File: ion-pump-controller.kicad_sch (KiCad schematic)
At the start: 48 parts, among them J1 Barrel_Jack, J2 Conn_02x04_Counter_Clockwise, Q1 IRFP4668PbF, T1 Transformer_1P_1S, U1 TSR_1-2433, U2 MCP6001R, U3 TC4422, U4 TSR1.5-24120E

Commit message: 1.0 version
these are the new schematic and pcb files for what should be the theoretically working board
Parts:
- removed J2: Conn_02x04_Counter_Clockwise, symbol Connector_Generic:Conn_02x04_Counter_Clockwise
- removed U3: TC4422, Package_DIP:DIP-8_W7.62mm, symbol Driver_FET:TC4422
- added C9: 2.5nf, Capacitor_THT:C_Disc_D14.5mm_W5.0mm_P10.00mm, symbol Device:C
- added D9: UF5408, Diode_THT:D_DO-201AD_P15.24mm_Horizontal, symbol Diode:UF5408
- added J2: START BUTTON, TerminalBlock_Phoenix:TerminalBlock_Phoenix_MKDS-1,5-2_1x02_P5.00mm_Horizontal, symbol Connector:Conn_01x02_Pin
- added J3: SCREEN, Connector_Phoenix_SPT:PhoenixContact_SPT_2.5_4-H-5.0_1x04_P5.0mm_Horizontal, symbol Connector:Conn_01x04_Pin
- added J4: DRAIN BUTTON, TerminalBlock_Phoenix:TerminalBlock_Phoenix_MKDS-1,5-2_1x02_P5.00mm_Horizontal, symbol Connector:Conn_01x02_Pin
- added J5: LIGHT, TerminalBlock_Phoenix:TerminalBlock_Phoenix_MKDS-1,5-2_1x02_P5.00mm_Horizontal, symbol Connector:Conn_01x02_Pin
- added J6: POWER SWITCH, TerminalBlock_Phoenix:TerminalBlock_Phoenix_MKDS-1,5-2_1x02_P5.00mm_Horizontal, symbol Connector:Conn_01x02_Pin
- added R22, R23: 330, Resistor_THT:R_Axial_DIN0411_L9.9mm_D3.6mm_P25.40mm_Horizontal, symbol Device:R
- added R24: 1k, Resistor_THT:R_Axial_DIN0411_L9.9mm_D3.6mm_P25.40mm_Horizontal, symbol Device:R
- added R25: 47k, Resistor_THT:R_Axial_DIN0411_L9.9mm_D3.6mm_P25.40mm_Horizontal, symbol Device:R
- added U5: 6N137, Package_DIP:DIP-8_W7.62mm, symbol Isolator:6N137
- added U6: TC4421, Package_DIP:DIP-8_W7.62mm, symbol Driver_FET:TC4421
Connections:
- net +12V: now also U6.1 (VDD), U6.8 (VDD)
- net +24V: now also C9.1, J6.1 (Pin_1), R25.1; no longer J1.1
- net +3V3: now also J3.1 (Pin_1), R24.2, U5.7 (EN), U5.8 (VCC)
- net GND: now also J2.2 (Pin_2), J3.4 (Pin_4), J4.2 (Pin_2), J5.2 (Pin_2), U5.3 (C), U5.5 (GND), U6.4 (GND), U6.5 (GND)
- net PWM output: now also R23.2, U5.2 (A); no longer A1.5 (DAC2/A0)
- net at A1.17 (SDA/IO23): now also J3.2 (Pin_2)
- net at A1.18 (SCL/IO22): now also J3.3 (Pin_3)
- net at A1.19 (A6/IO14): now also J2.1 (Pin_1)
- net at A1.20 (A7/IO32): now also J4.1 (Pin_1)
- net at A1.23 (A10/IO27): now also R22.1
- net at Q1.1 (G): now also U6.6 (~{OUTPUT}), U6.7 (~{OUTPUT})
- net at Q1.2 (D), T1.2 (AB): now also D9.2 (A)
- new net: R24.1, U5.6 (VO), U6.2 (INPUT)
- new net: A1.5 (DAC2/A0), R23.1
- new net: J1.1, J6.2 (Pin_2)
- new net: C9.2, D9.1 (K), R25.2
- new net: J5.1 (Pin_1), R22.2
- no-connect marks 17 -> 18
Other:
- note added: "EVIL ASS HIGH VOLTAGE OWIE"
- note added: "MOCK - DIFFERENT WHEN REALIZED"
- note added: "THERE IS NO OUTPUT PUT THE OUTPUT TYPE YOU NEED FOR YOUR ION PUMP HERE"
- note added: "screen mock"
- note removed: "ADD 1 SCREEN WITH 4 LINES ADD 1 SWITCH FOR POWER ADD 2 BUTTONS FOR GO/DRAIN START - PIN 14 DRAIN - PIN 32 LIGHT - PIN 27 SCREEN - PIN 23, 22, VCC, GND"
- moved on the sheet: Q1, T1, U4

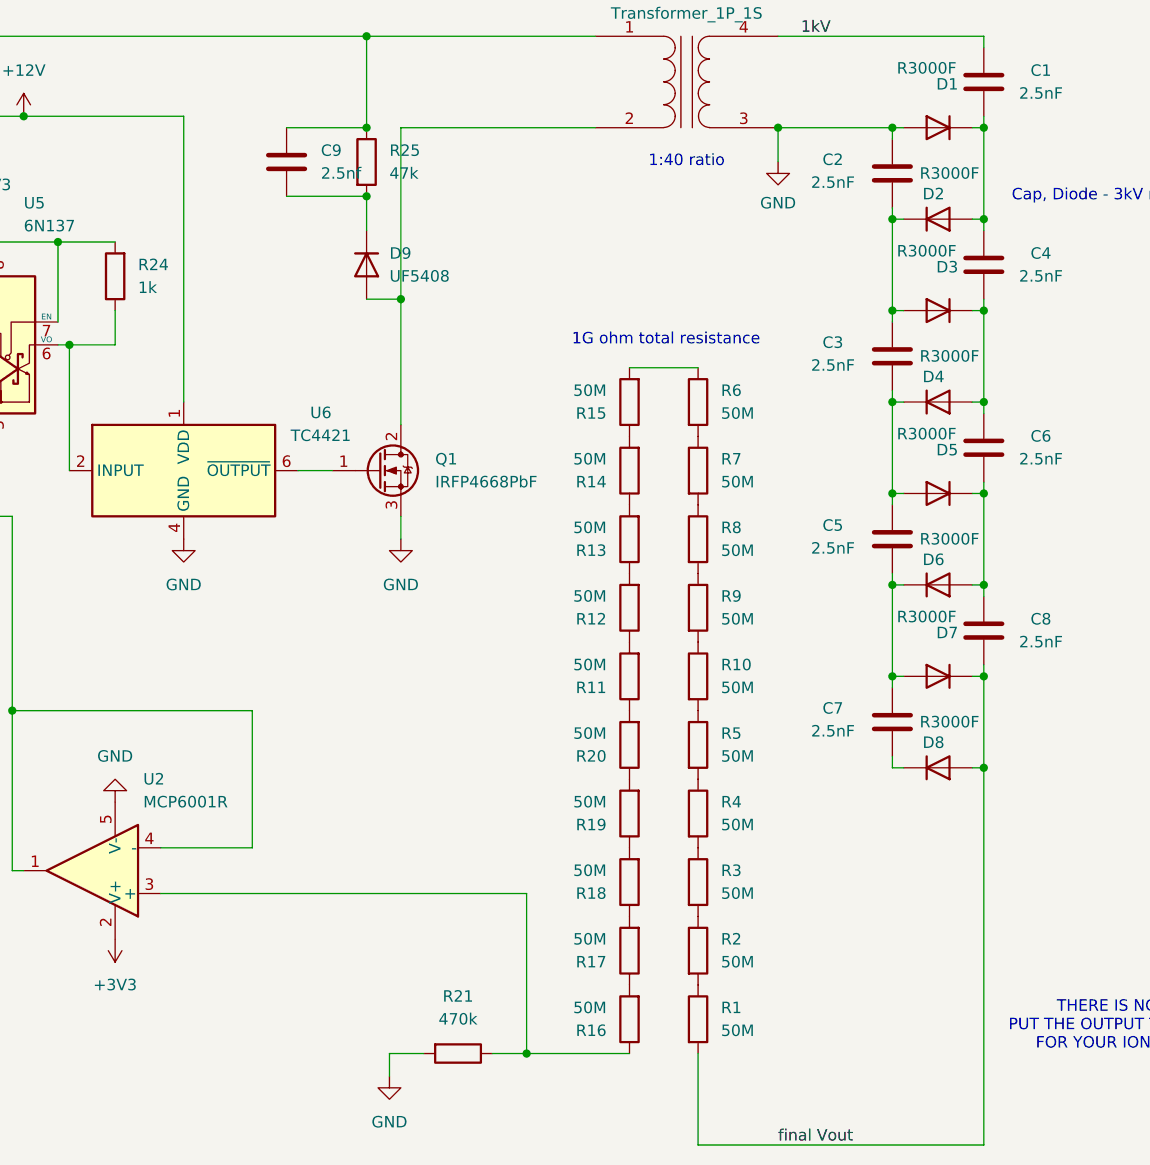
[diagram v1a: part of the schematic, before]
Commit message: v1.1
split the ground plane to high and low voltage, made the output two pads instead of screw terminals
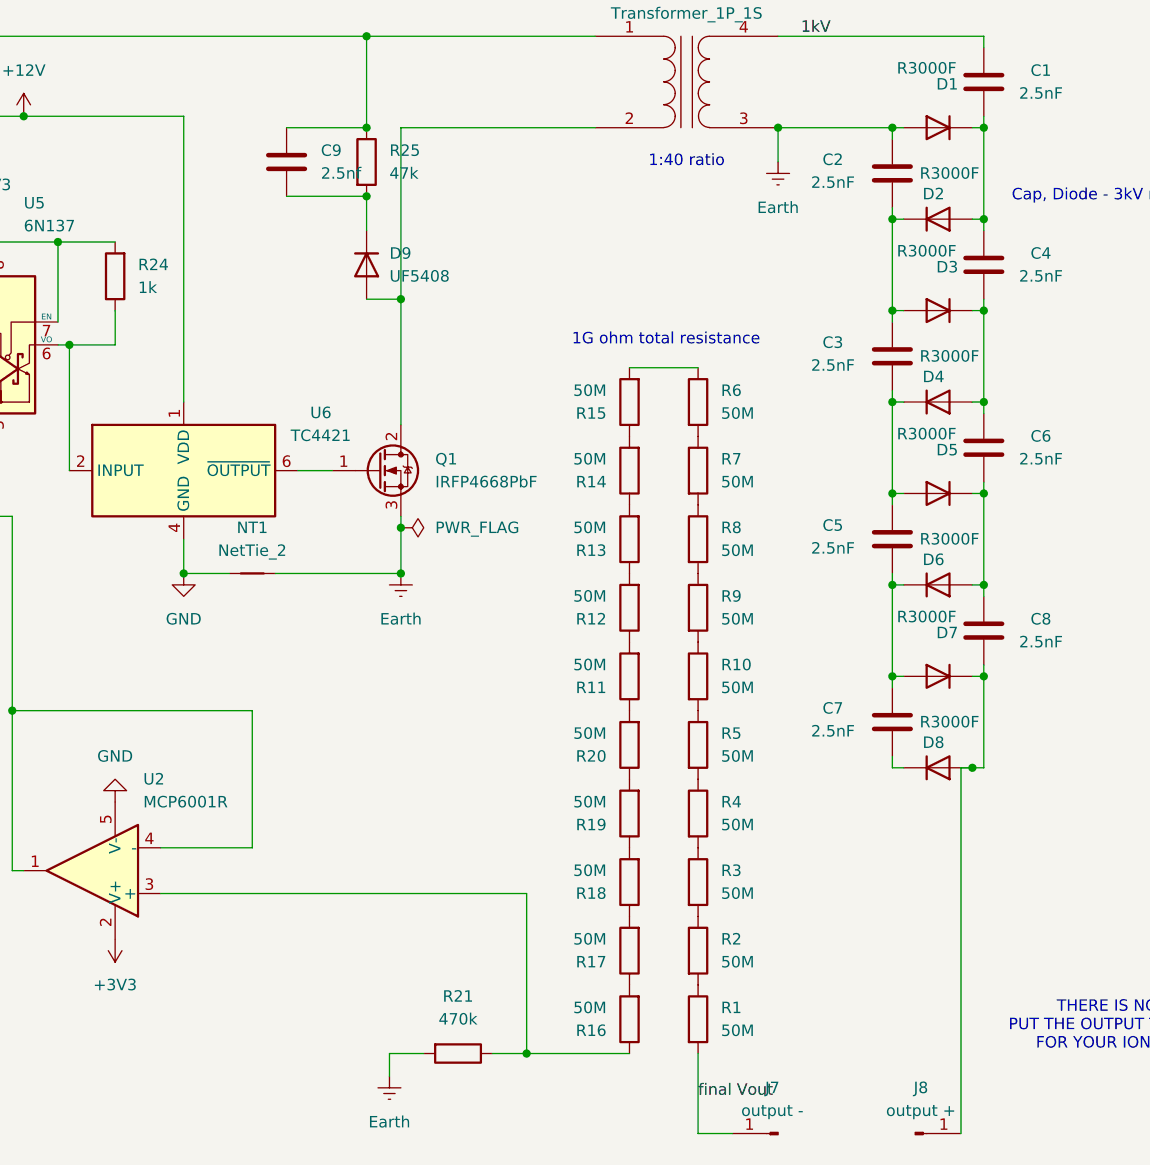
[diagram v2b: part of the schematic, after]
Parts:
- added J7: output -, TestPoint:TestPoint_Pad_4.0x4.0mm, symbol Connector:Conn_01x01_Pin
- added J8: output +, TestPoint:TestPoint_Pad_4.0x4.0mm, symbol Connector:Conn_01x01_Pin
- added NT1: NetTie_2, NetTie:NetTie-2_SMD_Pad2.0mm, symbol Device:NetTie_2
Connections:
- net GND: now also NT1.1; no longer C2.2, D1.2 (A), Q1.3 (S), R21.2, T1.3 (SA)
- net final Vout: now also J7.1 (Pin_1); no longer C8.1, D7.1 (K), D8.2 (A)
- new net: C8.1, D7.1 (K), D8.2 (A), J8.1 (Pin_1)
- new net Earth: C2.2, D1.2 (A), NT1.2, Q1.3 (S), R21.2, T1.3 (SA)

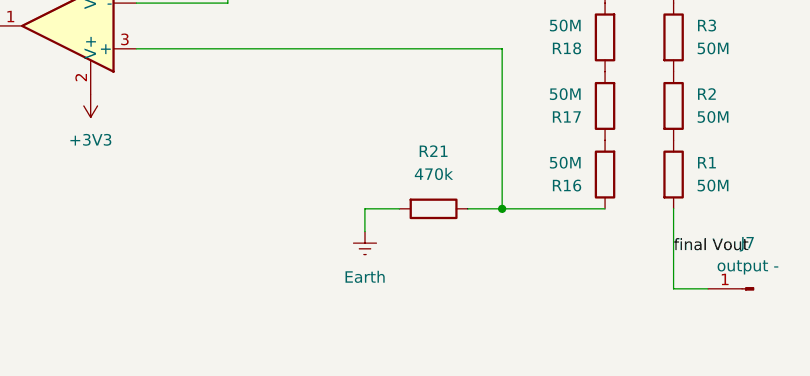
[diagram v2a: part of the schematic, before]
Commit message: v1.1
added a pad for earth gnd
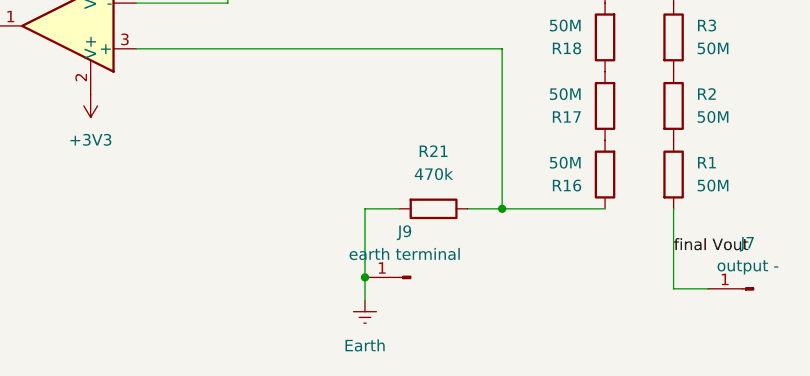
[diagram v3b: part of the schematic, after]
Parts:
- added J9: earth terminal, TestPoint:TestPoint_Pad_4.0x4.0mm, symbol Connector:Conn_01x01_Pin
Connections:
- net Earth: now also J9.1 (Pin_1)
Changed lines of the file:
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@@
 	)
 	(junction
+		(at 182.88 158.75)
+		(diameter 0)
+		(color 0 0 0 0)
+	)
+	(junction
 		(at 59.69 38.1)
 		(diameter 0)
@@
 	(wire
 		(pts
-			(xy 182.88 151.13) (xy 182.88 153.67)
+			(xy 182.88 151.13) (xy 182.88 158.75)
 		)
 		(stroke
@@
 	(wire
 		(pts
+			(xy 182.88 158.75) (xy 182.88 161.29)
+		)
+		(stroke
+			(width 0)
+			(type default)
+		)
+	)
+	(wire
+		(pts
 			(xy 133.35 96.52) (xy 107.95 96.52)
 		)
@@
 	(symbol
 		(lib_id "power:Earth")
-		(at 182.88 153.67 0)
+		(at 182.88 161.29 0)
 		(unit 1)
 		(exclude_from_sim no)
@@
 		(fields_autoplaced yes)
 		(property "Reference" "#PWR025"
-			(at 182.88 160.02 0)
+			(at 182.88 167.64 0)
 			(effects
 				(font
@@
 		)
 		(property "Value" "Earth"
-			(at 182.88 158.75 0)
+			(at 182.88 166.37 0)
 			(effects
 				(font
@@
 		)
 		(property "Footprint" ""
-			(at 182.88 153.67 0)
+			(at 182.88 161.29 0)
 			(effects
 				(font
@@
 		)
 		(property "Datasheet" "~"
-			(at 182.88 153.67 0)
+			(at 182.88 161.29 0)
 			(effects
 				(font
@@
 		)
 		(property "Description" "Power symbol creates a global label with name \"Earth\""
-			(at 182.88 153.67 0)
+			(at 182.88 161.29 0)
 			(effects
 				(font
@@
 					(unit 1)
 				)
+			)
+		)
+	)
+	(symbol
+		(lib_id "Connector:Conn_01x01_Pin")
+		(at 187.96 158.75 180)
+		(unit 1)
+		(exclude_from_sim no)
+		(in_bom yes)
+		(on_board yes)
+		(dnp no)
+		(fields_autoplaced yes)
+		(property "Reference" "J9"
+			(at 187.325 153.67 0)
+			(effects
+				(font
+					(size 1.27 1.27)
+				)
+			)
+		)
+		(property "Value" "earth terminal"
+			(at 187.325 156.21 0)
+			(effects
+				(font
+					(size 1.27 1.27)
+				)
+			)
+		)
+		(property "Footprint" "TestPoint:TestPoint_Pad_4.0x4.0mm"
+			(at 187.96 158.75 0)
+			(effects
+				(font
+					(size 1.27 1.27)
+				)
+				(hide yes)
+			)
+		)
+		(property "Datasheet" "~"
+			(at 187.96 158.75 0)
+			(effects
+				(font
+					(size 1.27 1.27)
+				)
+				(hide yes)
+			)
+		)
+		(property "Description" "Generic connector, single row, 01x01, script generated"
+			(at 187.96 158.75 0)
+			(effects
+				(font
+					(size 1.27 1.27)
+				)
+				(hide yes)
+			)
+		)
+		(pin "1"
+		)
+		(instances
+			(project "ion-pump-controller"
+				(path "/b810c8e2-bee1-4756-9807-978788334584"
+					(reference "J9")
+					(unit 1)
+				)
